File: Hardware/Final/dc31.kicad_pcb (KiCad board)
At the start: 2 copper layers, 109.7 x 109.5 mm, 72 parts, among them J1 OLED, J2 SYNC OUT, J3 FRONT, J4 SYNC IN, J5 MIDI IN, J6 MIDI OUT, J7 Eurorack, J8 HEADPHONE, J9 Micro_SD_Card_SPI, Q1 3904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

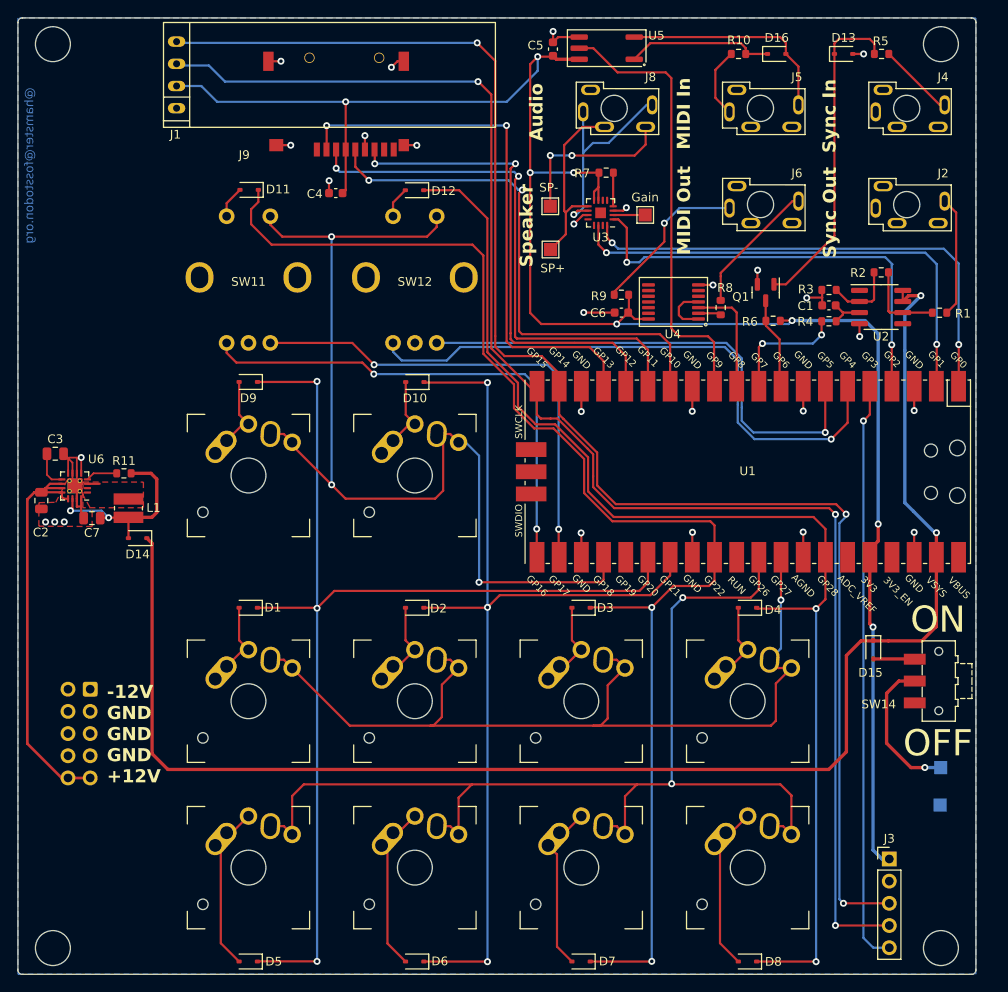
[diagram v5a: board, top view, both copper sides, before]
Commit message: Updated some 3D models Updated BOM sheet Added bodge instructions Added some documentation
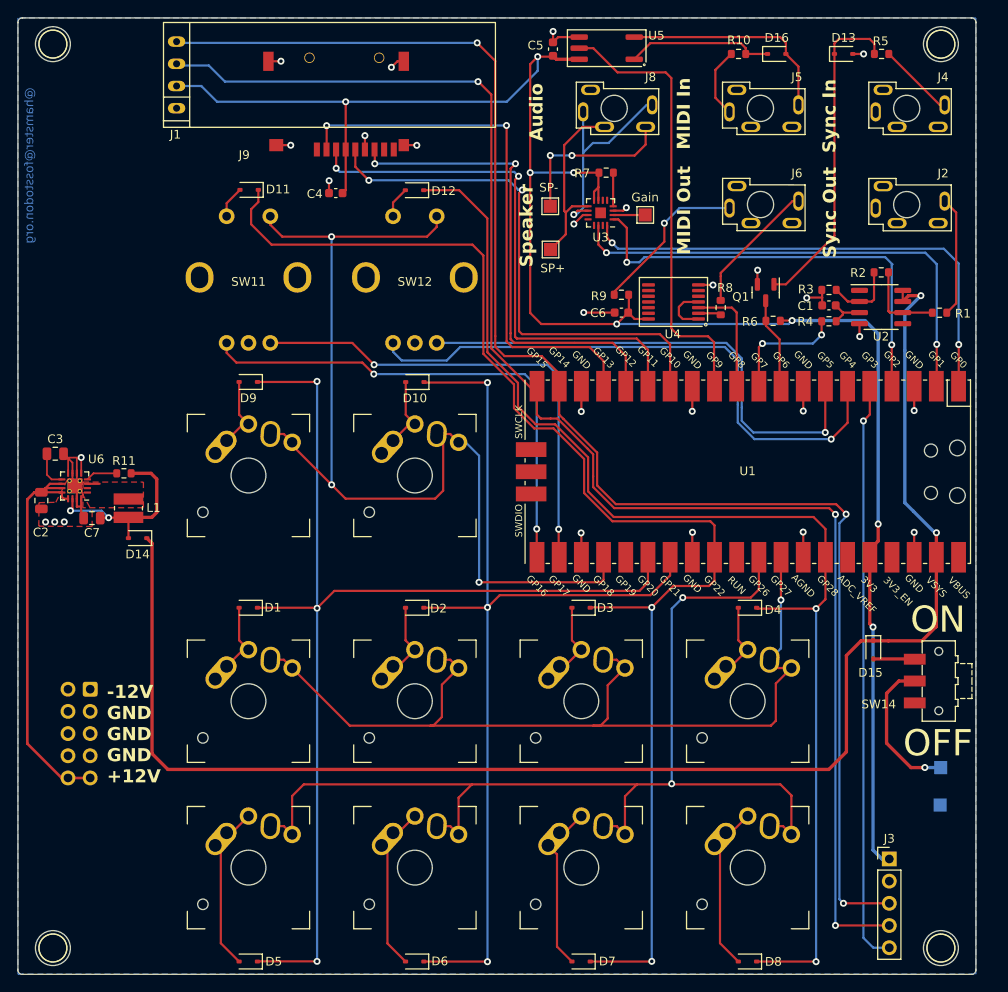
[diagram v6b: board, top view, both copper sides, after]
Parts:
- added HOLE1: MountingHole_1.6, lib_fp:MountingHole_1.6, F.Cu at (101.3, 147.3)
- added HOLE2: MountingHole_1.6, lib_fp:MountingHole_1.6, F.Cu at (101.3, 43.9)
- added HOLE3: MountingHole_1.6, lib_fp:MountingHole_1.6, F.Cu at (203.0, 43.9)
- added HOLE4: MountingHole_1.6, lib_fp:MountingHole_1.6, F.Cu at (203.0, 147.3)
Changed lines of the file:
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@@
     )
     (pad_to_mask_clearance 0)
+    (aux_axis_origin 97.32 150.34)
     (pcbplotparams
       (layerselection 0x00310fc_ffffffff)
@@
     (pad "2" thru_hole circle (at 0 -5.9) (size 2 2) (drill 1.2) (layers "*.Cu" "*.Mask")
       (net 59 "Net-(D1-A)") (pinfunction "2") (pintype "passive"))
-    (model "${KIPRJMOD}/3d/MX_WithCap.STEP"
+    (model "${KIPRJMOD}/3d/MX_WithFlatCap.STEP"
       (offset (xyz 7.35 7.35 6))
       (scale (xyz 1 1 1))
@@
     )
   )
+  (footprint "lib_fp:MountingHole_1.6" (layer "F.Cu")
+    (at 101.32 43.85)
+    (attr smd)
+    (fp_text reference "HOLE2" (at 0.0508 -3.2766 unlocked) (layer "F.SilkS") hide
+        (effects (font (size 1 1) (thickness 0.15)))
+    )
+    (fp_text value "MountingHole_1.6" (at 0 3.2512 unlocked) (layer "F.Fab") hide
+        (effects (font (size 1 1) (thickness 0.15)))
+    )
+    (fp_text user "${REFERENCE}" (at 0.0254 4.8514 unlocked) (layer "F.Fab") hide
+        (effects (font (size 1 1) (thickness 0.15)))
+    )
+    (fp_circle (center 0 0) (end 1.6 0)
+      (stroke (width 0.12) (type default)) (fill none) (layer "F.SilkS"))
+    (pad "" np_thru_hole circle (at 0 0) (size 3.2 3.2) (drill 3.2) (layers "F&B.Cu" "*.Mask"))
+  )
   (footprint "lib_fp:RotaryEncoder" (layer "F.Cu")
     (at 142.76 70.56)
@@
     (pad "S2" thru_hole circle (at 2.5 -7) (size 1.8 1.8) (drill 1) (layers "*.Cu" "*.Mask")
       (net 51 "C2") (pinfunction "S2") (pintype "passive"))
-    (model "${KIPRJMOD}/3d/Rotary_Encoder_With_Knob.STEP"
+    (model "${KIPRJMOD}/3d/Rotary_Encoder_With_Black_Knob.STEP"
       (offset (xyz 6.7 -6.3 0.5))
       (scale (xyz 1 1 1))
@@
     )
   )
+  (footprint "lib_fp:MountingHole_1.6" (layer "F.Cu")
+    (at 101.32 147.33)
+    (attr smd)
+    (fp_text reference "HOLE1" (at 0.0508 -3.2766 unlocked) (layer "F.SilkS") hide
+        (effects (font (size 1 1) (thickness 0.15)))
+    )
+    (fp_text value "MountingHole_1.6" (at 0 3.2512 unlocked) (layer "F.Fab") hide
+        (effects (font (size 1 1) (thickness 0.15)))
+    )
+    (fp_text user "${REFERENCE}" (at 0.0254 4.8514 unlocked) (layer "F.Fab") hide
+        (effects (font (size 1 1) (thickness 0.15)))
+    )
+    (fp_circle (center 0 0) (end 1.6 0)
+      (stroke (width 0.12) (type default)) (fill none) (layer "F.SilkS"))
+    (pad "" np_thru_hole circle (at 0 0) (size 3.2 3.2) (drill 3.2) (layers "F&B.Cu" "*.Mask"))
+  )
   (footprint "Resistor_SMD:R_0603_1608Metric" (layer "F.Cu")
     (at 109.45 92.99)
@@
     (pad "2" thru_hole circle (at 0 -5.9) (size 2 2) (drill 1.2) (layers "*.Cu" "*.Mask")
       (net 66 "Net-(D8-A)") (pinfunction "2") (pintype "passive"))
-    (model "${KIPRJMOD}/3d/MX_WithCap.STEP"
+    (model "${KIPRJMOD}/3d/MX_WithFlatCap.STEP"
       (offset (xyz 7.35 7.35 6))
       (scale (xyz 1 1 1))
@@
     (pad "2" thru_hole circle (at 0 -5.9) (size 2 2) (drill 1.2) (layers "*.Cu" "*.Mask")
       (net 65 "Net-(D7-A)") (pinfunction "2") (pintype "passive"))
-    (model "${KIPRJMOD}/3d/MX_WithCap.STEP"
+    (model "${KIPRJMOD}/3d/MX_WithFlatCap.STEP"
       (offset (xyz 7.35 7.35 6))
       (scale (xyz 1 1 1))
@@
     (pad "2" thru_hole circle (at 0 -5.9) (size 2 2) (drill 1.2) (layers "*.Cu" "*.Mask")
       (net 61 "Net-(D3-A)") (pinfunction "2") (pintype "passive"))
-    (model "${KIPRJMOD}/3d/MX_WithCap.STEP"
+    (model "${KIPRJMOD}/3d/MX_WithFlatCap.STEP"
       (offset (xyz 7.35 7.35 6))
       (scale (xyz 1 1 1))
@@
     )
   )
+  (footprint "lib_fp:MountingHole_1.6" (layer "F.Cu")
+    (at 202.98 147.34)
+    (attr smd)
+    (fp_text reference "HOLE4" (at 0.0508 -3.2766 unlocked) (layer "F.SilkS") hide
+        (effects (font (size 1 1) (thickness 0.15)))
+    )
+    (fp_text value "MountingHole_1.6" (at 0 3.2512 unlocked) (layer "F.Fab") hide
+        (effects (font (size 1 1) (thickness 0.15)))
+    )
+    (fp_text user "${REFERENCE}" (at 0.0254 4.8514 unlocked) (layer "F.Fab") hide
+        (effects (font (size 1 1) (thickness 0.15)))
+    )
+    (fp_circle (center 0 0) (end 1.6 0)
+      (stroke (width 0.12) (type default)) (fill none) (layer "F.SilkS"))
+    (pad "" np_thru_hole circle (at 0 0) (size 3.2 3.2) (drill 3.2) (layers "F&B.Cu" "*.Mask"))
+  )
   (footprint "TestPoint:TestPoint_Pad_1.5x1.5mm" (layer "F.Cu")
     (at 158.29 67.37 180)
@@
     (pad "2" thru_hole circle (at 0 -5.9) (size 2 2) (drill 1.2) (layers "*.Cu" "*.Mask")
       (net 60 "Net-(D2-A)") (pinfunction "2") (pintype "passive"))
-    (model "${KIPRJMOD}/3d/MX_WithCap.STEP"
+    (model "${KIPRJMOD}/3d/MX_WithFlatCap.STEP"
       (offset (xyz 7.35 7.35 6))
       (scale (xyz 1 1 1))
@@
     (pad "2" thru_hole circle (at 0 -5.9) (size 2 2) (drill 1.2) (layers "*.Cu" "*.Mask")
       (net 63 "Net-(D5-A)") (pinfunction "2") (pintype "passive"))
-    (model "${KIPRJMOD}/3d/MX_WithCap.STEP"
+    (model "${KIPRJMOD}/3d/MX_WithFlatCap.STEP"
       (offset (xyz 7.35 7.35 6))
       (scale (xyz 1 1 1))
@@
     (pad "2" thru_hole circle (at 0 -5.9) (size 2 2) (drill 1.2) (layers "*.Cu" "*.Mask")
       (net 67 "Net-(D9-A)") (pinfunction "2") (pintype "passive"))
-    (model "${KIPRJMOD}/3d/MX_WithCap.STEP"
+    (model "${KIPRJMOD}/3d/MX_WithFlatCap.STEP"
       (offset (xyz 7.35 7.35 6))
       (scale (xyz 1 1 1))
@@
     )
   )
+  (footprint "lib_fp:MountingHole_1.6" (layer "F.Cu")
+    (at 202.98 43.86)
+    (attr smd)
+    (fp_text reference "HOLE3" (at 0.0508 -3.2766 unlocked) (layer "F.SilkS") hide
+        (effects (font (size 1 1) (thickness 0.15)))
+    )
+    (fp_text value "MountingHole_1.6" (at 0 3.2512 unlocked) (layer "F.Fab") hide
+        (effects (font (size 1 1) (thickness 0.15)))
+    )
+    (fp_text user "${REFERENCE}" (at 0.0254 4.8514 unlocked) (layer "F.Fab") hide
+        (effects (font (size 1 1) (thickness 0.15)))
+    )
+    (fp_circle (center 0 0) (end 1.6 0)
+      (stroke (width 0.12) (type default)) (fill none) (layer "F.SilkS"))
+    (pad "" np_thru_hole circle (at 0 0) (size 3.2 3.2) (drill 3.2) (layers "F&B.Cu" "*.Mask"))
+  )
   (footprint "Diode_SMD:D_SOD-323" (layer "F.Cu")
     (at 191.84 44.98)
@@
     (pad "S2" thru_hole circle (at 2.5 -7) (size 1.8 1.8) (drill 1) (layers "*.Cu" "*.Mask")
       (net 51 "C2") (pinfunction "S2") (pintype "passive"))
-    (model "${KIPRJMOD}/3d/Rotary_Encoder_With_Knob.STEP"
-      (offset (xyz 6.7 -6.3 0.5))
+    (model "${KIPRJMOD}/3d/Rotary_Encoder_With_Black_Knob.STEP"
+      (offset (xyz 6.7 -6.3 0.1))
       (scale (xyz 1 1 1))
       (rotate (xyz 0 0 0))
@@
     (pad "2" thru_hole circle (at 0 -5.9) (size 2 2) (drill 1.2) (layers "*.Cu" "*.Mask")
       (net 62 "Net-(D4-A)") (pinfunction "2") (pintype "passive"))
-    (model "${KIPRJMOD}/3d/MX_WithCap.STEP"
+    (model "${KIPRJMOD}/3d/MX_WithFlatCap.STEP"
       (offset (xyz 7.35 7.35 6))
       (scale (xyz 1 1 1))
@@
     (pad "2" thru_hole circle (at 0 -5.9) (size 2 2) (drill 1.2) (layers "*.Cu" "*.Mask")
       (net 64 "Net-(D6-A)") (pinfunction "2") (pintype "passive"))
-    (model "${KIPRJMOD}/3d/MX_WithCap.STEP"
+    (model "${KIPRJMOD}/3d/MX_WithFlatCap.STEP"
       (offset (xyz 7.35 7.35 6))
       (scale (xyz 1 1 1))
@@
     (pad "2" thru_hole circle (at 0 -5.9) (size 2 2) (drill 1.2) (layers "*.Cu" "*.Mask")
       (net 5 "Net-(D10-A)") (pinfunction "2") (pintype "passive"))
-    (model "${KIPRJMOD}/3d/MX_WithCap.STEP"
+    (model "${KIPRJMOD}/3d/MX_WithFlatCap.STEP"
       (offset (xyz 7.35 7.35 6))
       (scale (xyz 1 1 1))
